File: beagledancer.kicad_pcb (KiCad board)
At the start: 2 copper layers, 32 x 23.1 mm, 12 parts, among them J1 USB-MICRO-B, P9 BeagleBone, U1 MAX3421, X1 XTAL4PIN

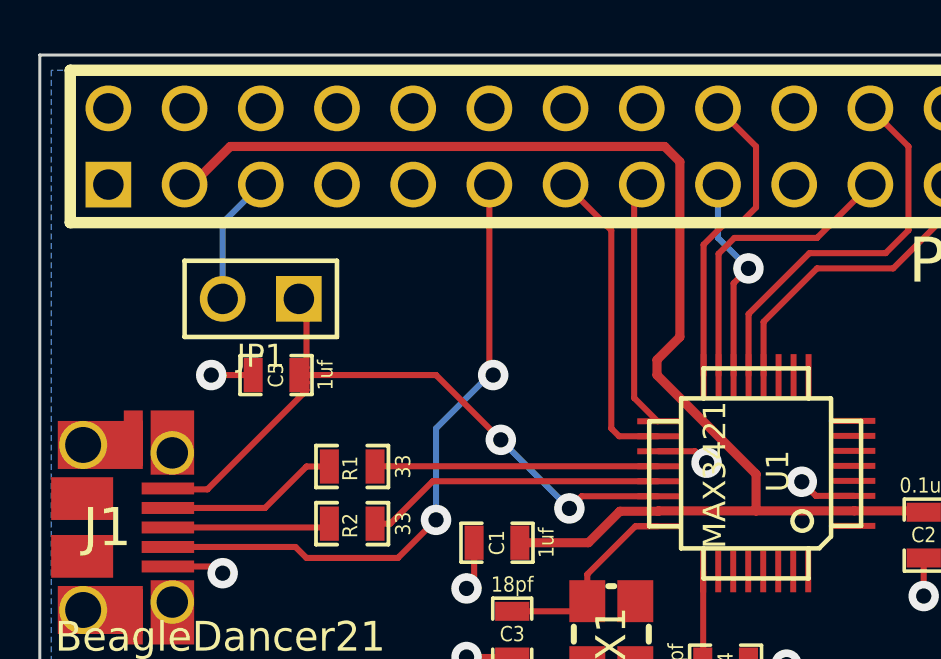
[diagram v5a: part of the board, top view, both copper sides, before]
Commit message: Tidy up 5V and 3.3V traces.
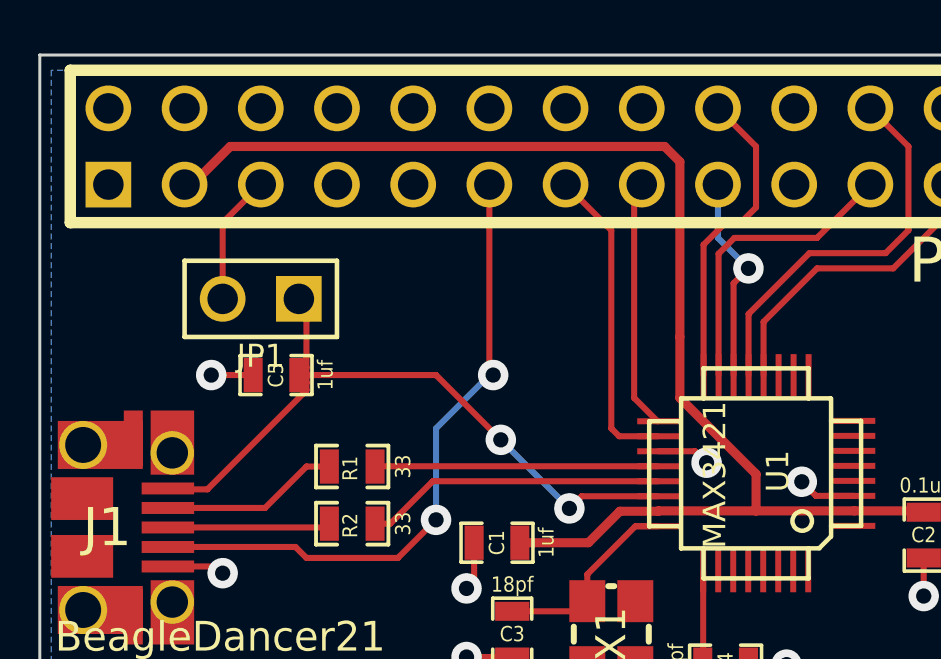
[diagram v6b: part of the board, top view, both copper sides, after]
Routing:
- net +3.3V: track 44.5 -> 43.9 mm
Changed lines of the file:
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@@
     (links 32)
     (no_connects 0)
-    (area 189.03957 135.0518 240.982431 160.708622)
+    (area 190.950427 135.0518 230.428001 160.708622)
     (thickness 1.6)
     (drawings 8)
-    (tracks 120)
+    (tracks 119)
     (zones 0)
     (modules 12)
@@
     (effects (font (size 0.992 0.9666) (thickness 0.16164)) (justify left))
   )
+  (segment (start 219.71 148.082) (end 219.71 146.05) (width 0.3048) (layer F.Cu) (net 1))
+  (segment (start 204.724 139.7) (end 219.202 139.7) (width 0.3048) (layer F.Cu) (net 1))
+  (segment (start 219.202 139.7) (end 219.71 140.208) (width 0.3048) (layer F.Cu) (net 1))
+  (segment (start 219.71 140.208) (end 219.71 146.05) (width 0.3048) (layer F.Cu) (net 1))
+  (segment (start 203.454 140.97) (end 204.724 139.7) (width 0.3048) (layer F.Cu) (net 1) (status 10))
+  (segment (start 203.454 140.97) (end 203.2 140.97) (width 0.3048) (layer F.Cu) (net 1) (status 30))
   (segment (start 225.525 151.847) (end 227.793 151.847) (width 0.3048) (layer F.Cu) (net 1))
   (segment (start 227.793 151.847) (end 227.838 151.892) (width 0.3048) (layer F.Cu) (net 1))
   (segment (start 216.662 152.908) (end 214.376 152.908) (width 0.3048) (layer F.Cu) (net 1))
-  (segment (start 203.2 140.97) (end 203.454 140.97) (width 0.3048) (layer F.Cu) (net 1) (status 30))
-  (segment (start 203.454 140.97) (end 204.724 139.7) (width 0.3048) (layer F.Cu) (net 1) (status 10))
   (segment (start 225.525 151.847) (end 222.25 151.847) (width 0.3048) (layer F.Cu) (net 1) (status 10))
   (segment (start 218.9875 151.8595) (end 217.7105 151.8595) (width 0.3048) (layer F.Cu) (net 1))
   (segment (start 217.7105 151.8595) (end 216.662 152.908) (width 0.3048) (layer F.Cu) (net 1))
   (segment (start 222.25 150.622) (end 222.25 151.847) (width 0.3048) (layer F.Cu) (net 1))
-  (segment (start 218.948 147.32) (end 222.25 150.622) (width 0.3048) (layer F.Cu) (net 1))
-  (segment (start 218.948 146.812) (end 218.948 147.32) (width 0.3048) (layer F.Cu) (net 1))
-  (segment (start 219.71 146.05) (end 218.948 146.812) (width 0.3048) (layer F.Cu) (net 1))
-  (segment (start 219.71 140.208) (end 219.71 146.05) (width 0.3048) (layer F.Cu) (net 1))
-  (segment (start 219.202 139.7) (end 219.71 140.208) (width 0.3048) (layer F.Cu) (net 1))
-  (segment (start 204.724 139.7) (end 219.202 139.7) (width 0.3048) (layer F.Cu) (net 1))
+  (segment (start 219.71 148.082) (end 222.25 150.622) (width 0.3048) (layer F.Cu) (net 1))
   (segment (start 222.25 151.847) (end 219 151.847) (width 0.3048) (layer F.Cu) (net 1) (status 20))
   (segment (start 219 151.847) (end 218.9875 151.8595) (width 0.3048) (layer F.Cu) (net 1) (status 30))
-  (segment (start 205.74 140.97) (end 204.47 142.24) (width 0.2032) (layer B.Cu) (net 2) (status 10))
-  (segment (start 204.47 142.24) (end 204.47 144.78) (width 0.2032) (layer B.Cu) (net 2) (status 20))
+  (segment (start 204.47 144.78) (end 204.47 142.24) (width 0.2032) (layer F.Cu) (net 2) (status 400000))
+  (segment (start 204.47 142.24) (end 205.74 140.97) (width 0.2032) (layer F.Cu) (net 2) (status 800000))
   (segment (start 218.9875 149.8595) (end 220.2175 149.8595) (width 0.2032) (layer F.Cu) (net 3))
   (via (at 220.599 150.241) (size 1.016) (layers F.Cu B.Cu) (net 3))

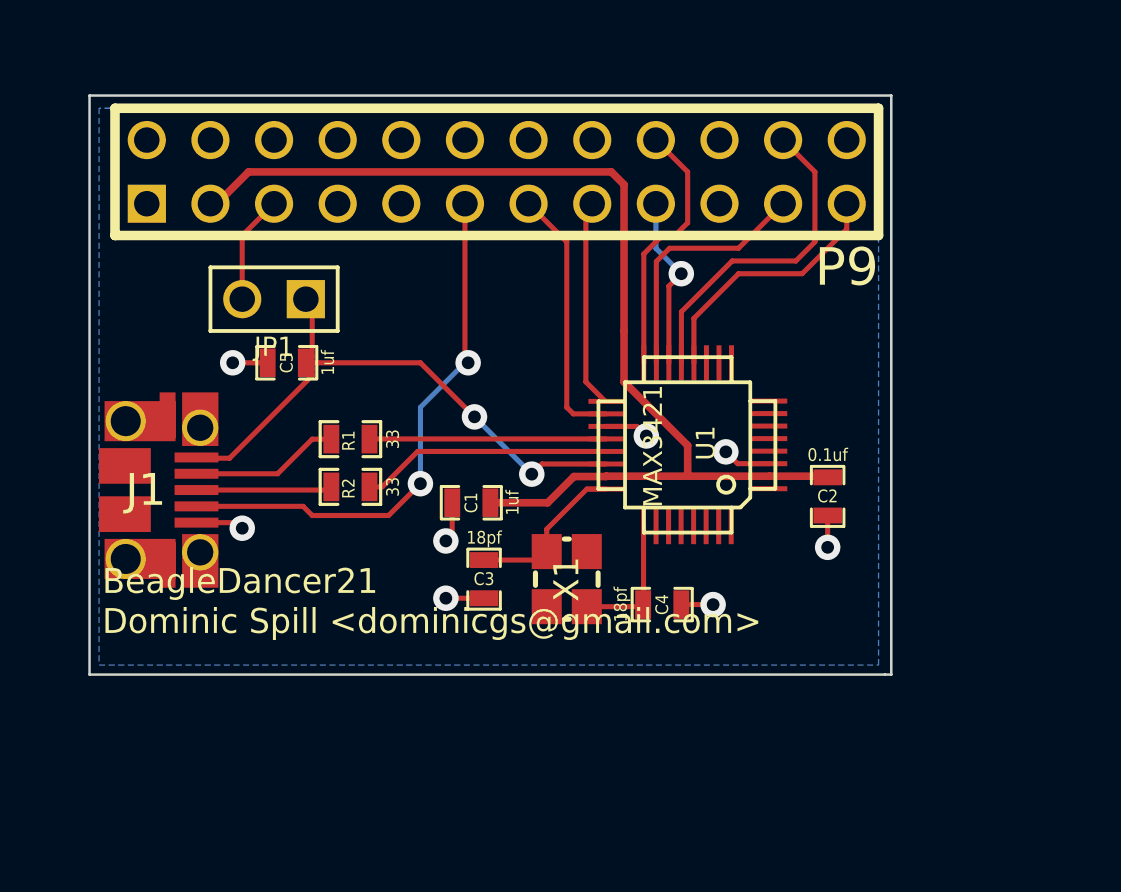
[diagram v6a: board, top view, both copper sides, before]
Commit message: Use bigger pads for the MAX3421 - as per land pattern.
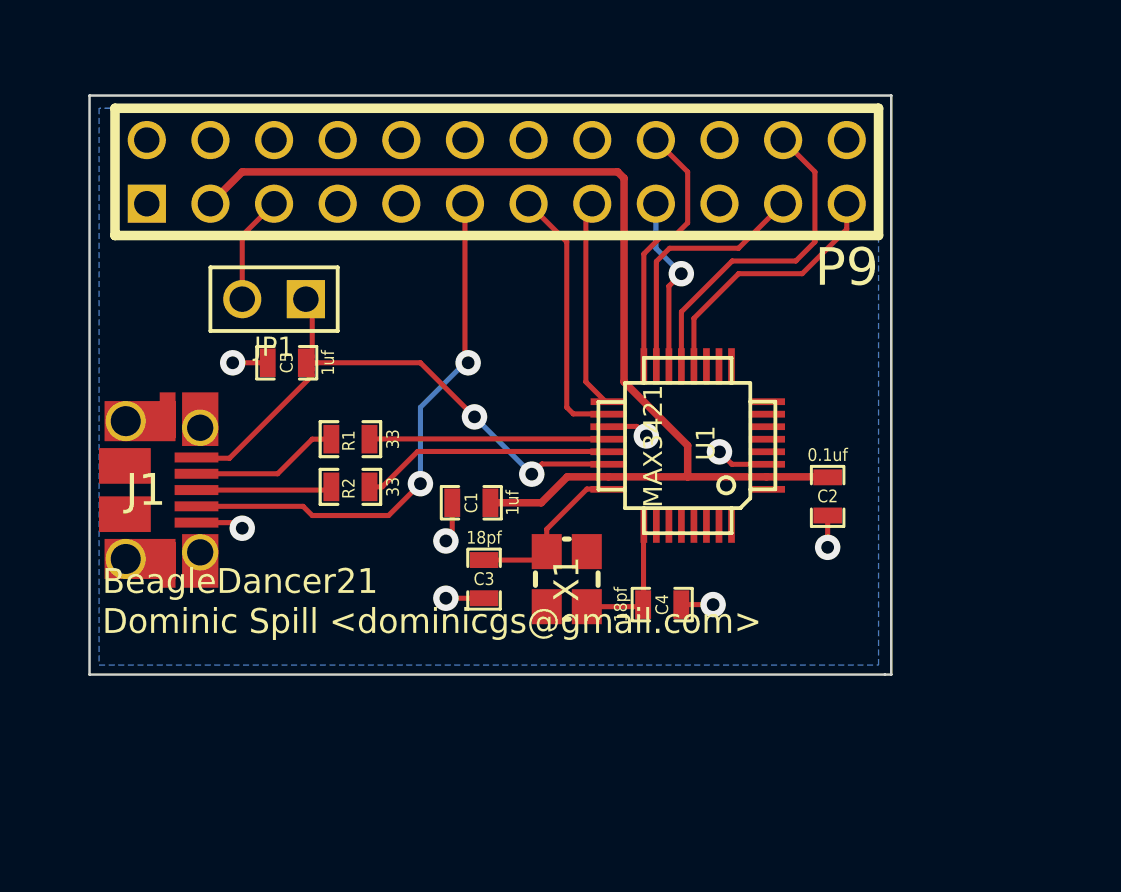
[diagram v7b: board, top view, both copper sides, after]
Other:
- net class Power: trace_width 0.3048 -> 0.3

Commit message: Swap C1/C2 to correct positions on schematic, named nets, ether tweaks.
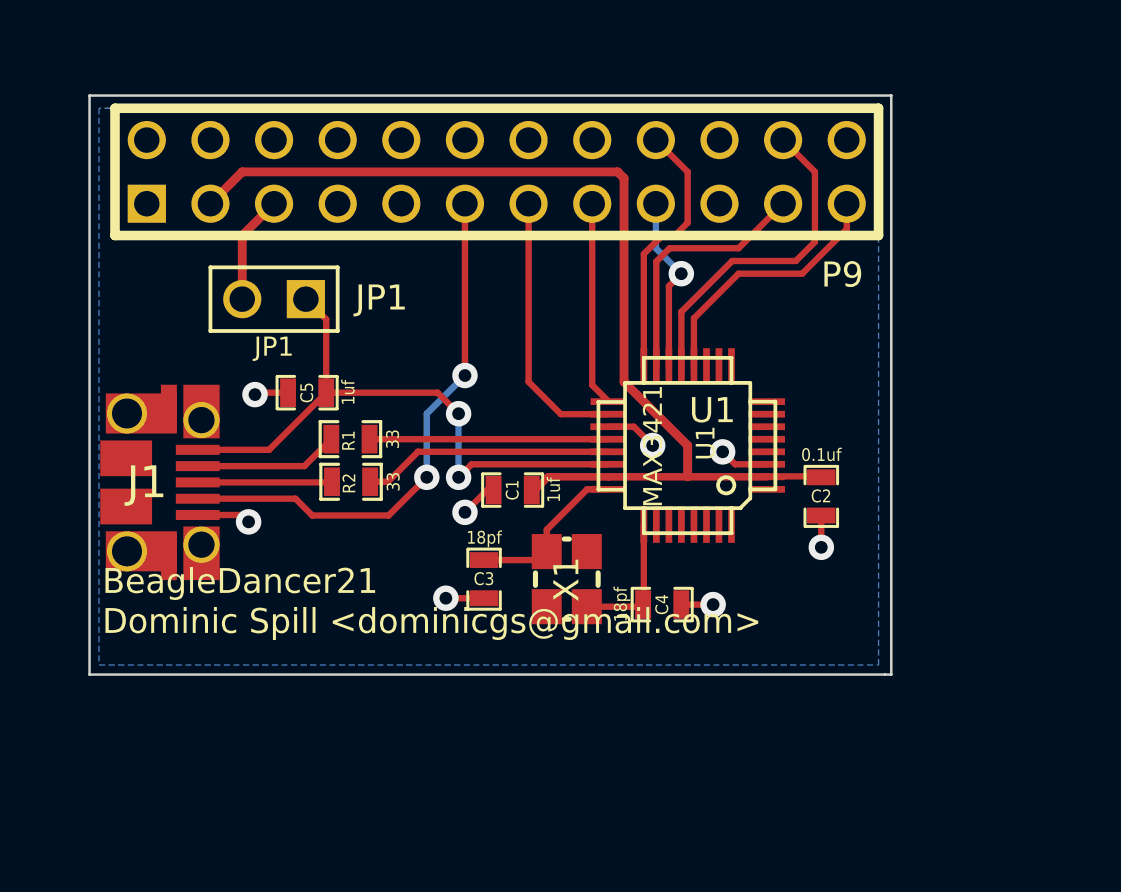
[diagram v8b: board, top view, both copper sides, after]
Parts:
- moved C1 1.73 mm to (215.3, 152.4)
- moved C5 1.44 mm to (207.1, 148.5)
- moved J1 0.31 mm to (198.2, 152.1)
- moved C2 0.25 mm to (227.6, 152.7)
- moved R2 0.20 mm to (208.8, 152.1)
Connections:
- net N-0000025 renamed /D+
- net N-0000026 renamed /D-
- net N-0000044 renamed /VBCOMP
- C3 pad 1: N-000002 (its old number) -> /XI
- C4 pad 1: N-000003 (its old number) -> /XO
- P9 pad 23: N-0000033 (its old number) -> /RES
- U1 pad 12: N-0000033 (its old number) -> /RES
- U1 pad 24: N-000002 (its old number) -> /XI
- U1 pad 25: N-000003 (its old number) -> /XO
- X1 pad 1: N-000002 (its old number) -> /XI
- X1 pad 3: N-000003 (its old number) -> /XO
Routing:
- net /XI: track 0.00 -> 13.5 mm
- net /RES: track 0.00 -> 12.3 mm
- net N-0000033 (its old number): track 10.4 -> 0.00 mm
- net /D-: track 9.44 -> 19.0 mm
- net /XO: track 0.00 -> 8.72 mm
- net N-000002 (its old number): track 6.88 -> 0.00 mm
- net SPI0_D1: track 10.4 -> 17.2 mm
- net N-000003 (its old number): track 5.40 -> 0.00 mm
- net SPI0_D0: track 10.1 -> 14.2 mm
- net SPI0_CS0: track 7.61 -> 10.8 mm
- net +3.3V: track 44.0 -> 41.8 mm
- net SPI0_SCLK: track 13.1 -> 15.3 mm
- net /VBCOMP: track 23.9 -> 24.5 mm
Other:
- net class Default: trace_width 0.2032 -> 0.254
- net class Power: trace_width 0.3 -> 0.3556
- board text added: "JP1"
- board text added: "U1"
